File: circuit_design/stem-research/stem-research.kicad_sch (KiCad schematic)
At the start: 11 parts, among them M1 Stepper_Motor_bipolar, M2 Stepper_Motor_bipolar, M3 Stepper_Motor_bipolar, M4 Fan, Q1 IRF540N

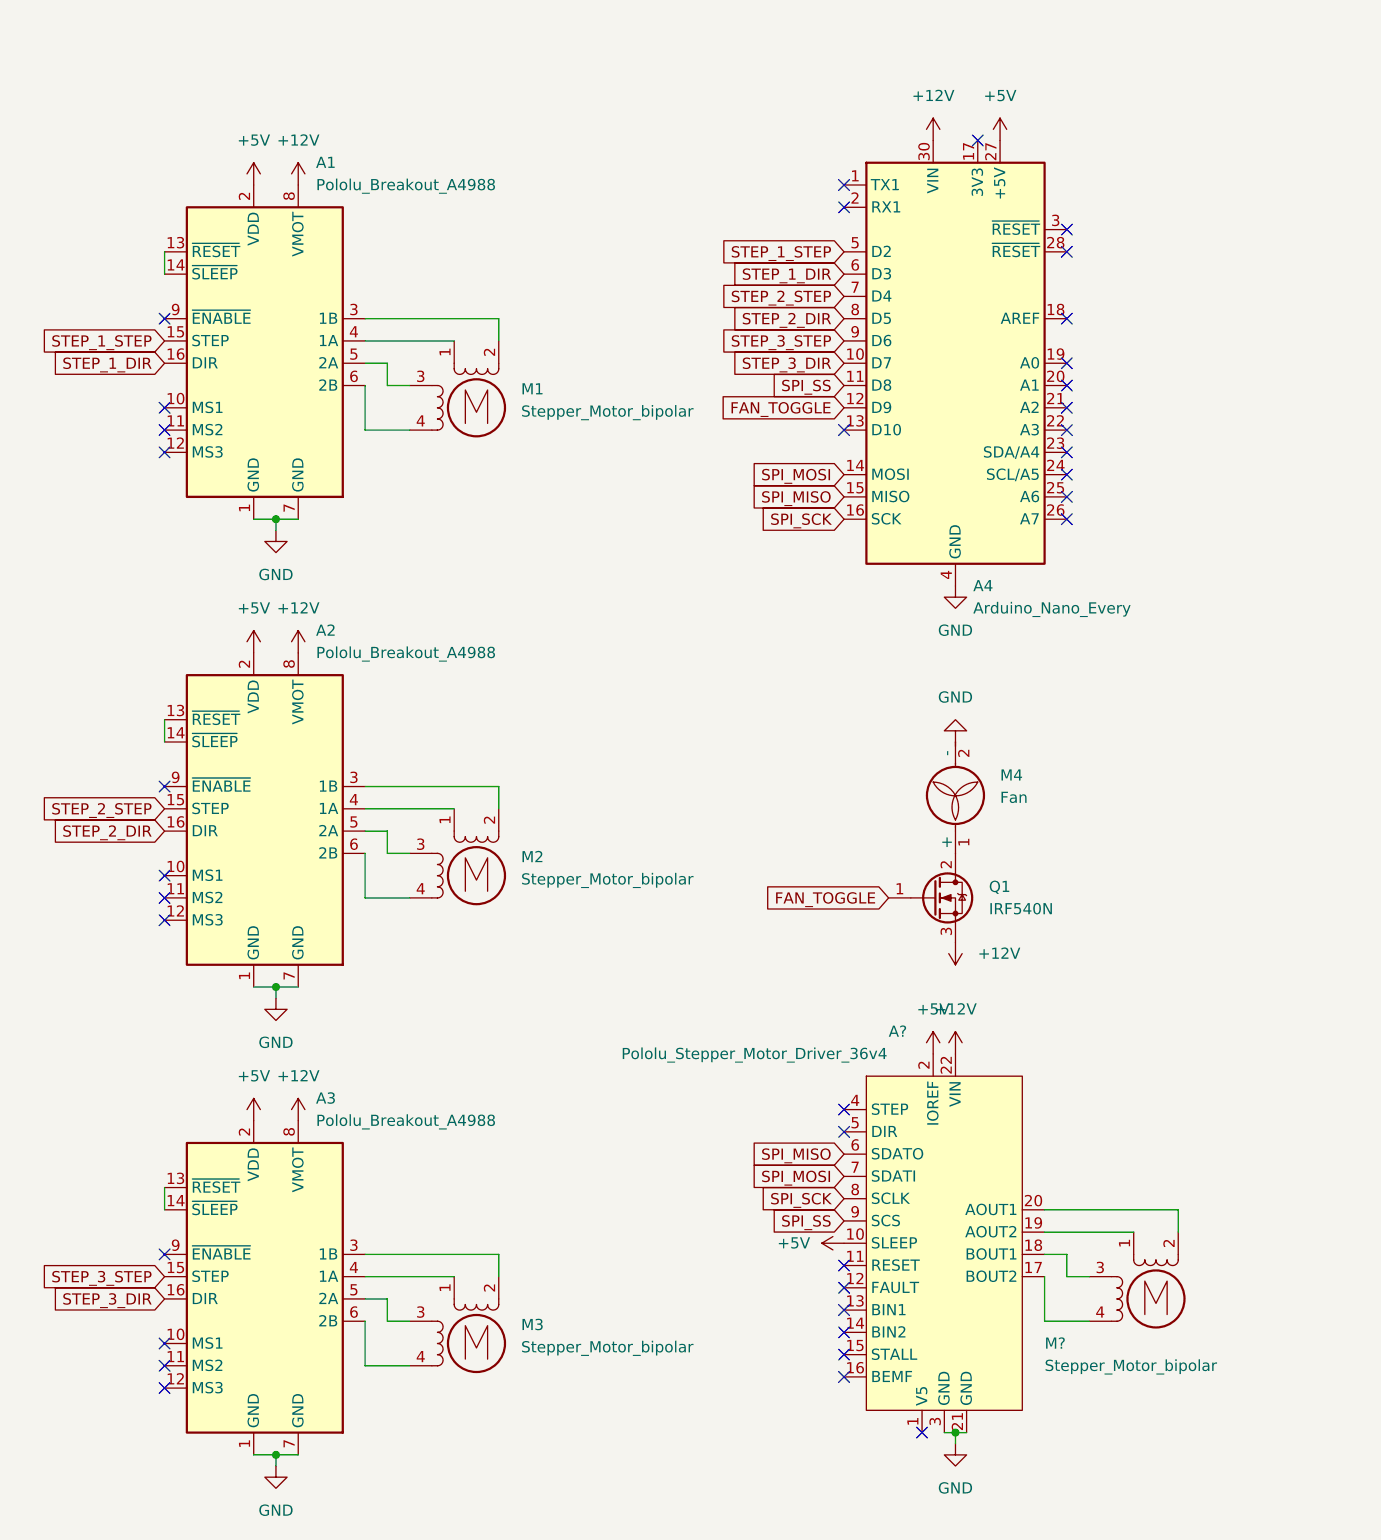
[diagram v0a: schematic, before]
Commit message: Replace Stepper Controlers and Switch to 24V
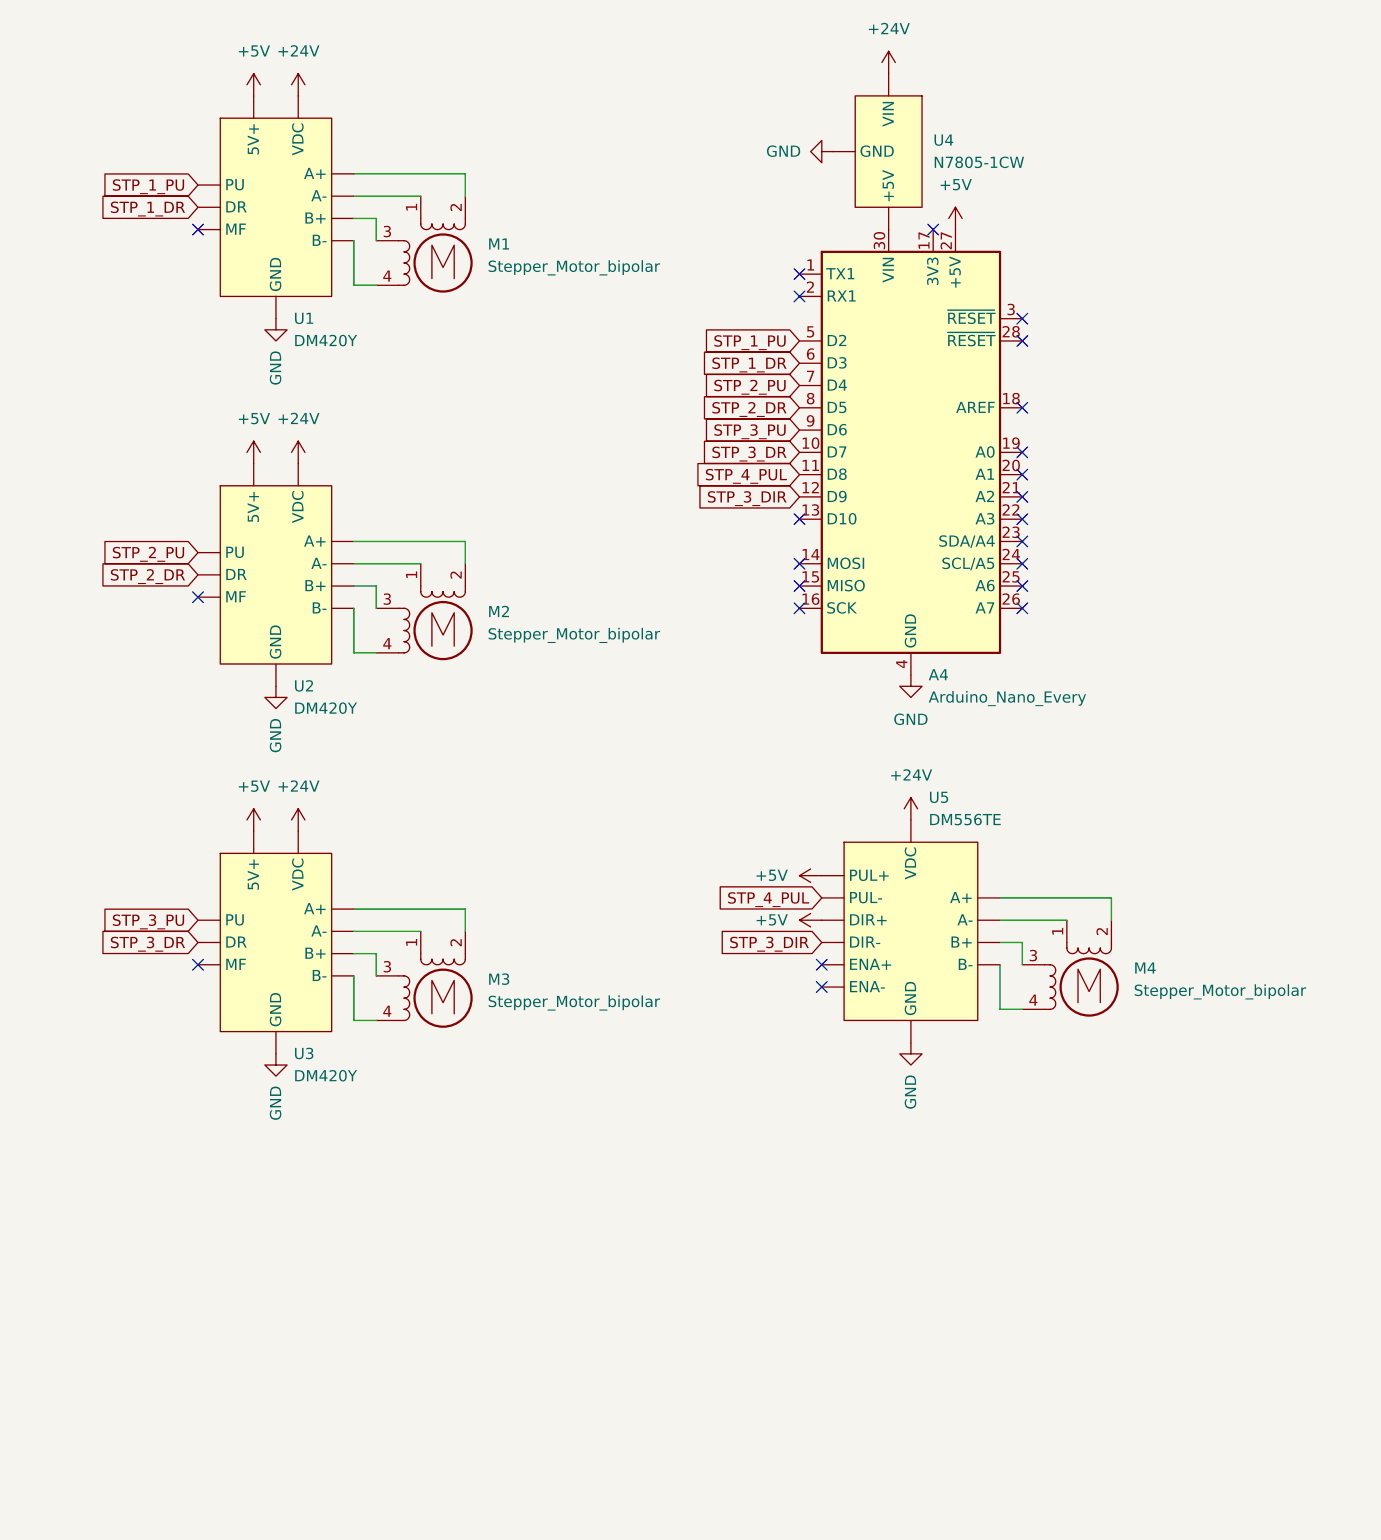
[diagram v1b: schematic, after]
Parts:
- removed A1, A2, A3: Pololu_Breakout_A4988, Module:Pololu_Breakout-16_15.2x20.3mm, symbol Driver_Motor:Pololu_Breakout_A4988
- removed A?: Pololu_Stepper_Motor_Driver_36v4, symbol custom:Pololu_Stepper_Motor_Driver_36v4
- removed M4: Fan, symbol Motor:Fan
- removed M?: Stepper_Motor_bipolar, symbol Motor:Stepper_Motor_bipolar
- removed Q1: IRF540N, Package_TO_SOT_THT:TO-220-3_Vertical, symbol Transistor_FET:IRF540N
- added M4: Stepper_Motor_bipolar, symbol Motor:Stepper_Motor_bipolar
- added U1, U2, U3: DM420Y, symbol custom:DM420Y
- added U4: N7805-1CW, symbol custom:N7805-1CW
- added U5: DM556TE, symbol custom:DM556TE
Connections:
- net +5V: now also U1. (VDC), U2. (VDC), U3. (VDC), U5. (VDC)
- net GND: now also U1. (VDC), U2. (VDC), U3. (VDC), U4. (VIN), U5. (VDC)
- net at M3.1: now also U3. (VDC)
- net at M3.2 (-): now also U3. (VDC)
- net at M3.3: now also U3. (VDC)
- net at M3.4: now also U3. (VDC)
- net at M2.2 (-): now also U2. (VDC)
- net at M2.1: now also U2. (VDC)
- net at M2.3: now also U2. (VDC)
- net at M2.4: now also U2. (VDC)
- net at M1.2 (-): now also U1. (VDC)
- net at M1.1: now also U1. (VDC)
- net at M1.3: now also U1. (VDC)
- net at M1.4: now also U1. (VDC)
- net +12V: no longer names the net of A4.30 (VIN)
- net +12V: now also U4. (VIN)
- net FAN_TOGGLE renamed STP_3_DIR
- net STP_3_DIR: now also U5. (VDC)
- net SPI_MISO: no longer names the net of A4.15 (MISO)
- net SPI_MOSI: no longer names the net of A4.14 (MOSI)
- net SPI_SCK: no longer names the net of A4.16 (SCK)
- net SPI_SS renamed STP_4_PUL
- net STP_4_PUL: now also U5. (VDC)
- net STEP_1_DIR renamed STP_1_DR
- net STP_1_DR: now also U1. (VDC)
- net STEP_1_STEP renamed STP_1_PU
- net STP_1_PU: now also U1. (VDC)
- net STEP_2_DIR renamed STP_2_DR
- net STP_2_DR: now also U2. (VDC)
- net STEP_2_STEP renamed STP_2_PU
- net STP_2_PU: now also U2. (VDC)
- net STEP_3_DIR renamed STP_3_DR
- net STP_3_DR: now also U3. (VDC)
- net STEP_3_STEP renamed STP_3_PU
- net STP_3_PU: now also U3. (VDC)
- new net: M4.1, U5. (VDC)
- new net: M4.2 (-), U5. (VDC)
- new net: M4.3, U5. (VDC)
- new net: M4.4, U5. (VDC)
- new net +24V: U1. (VDC), U2. (VDC), U3. (VDC), U4. (VIN), U5. (VDC)
- no-connect marks 36 -> 23
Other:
- moved on the sheet: A4
